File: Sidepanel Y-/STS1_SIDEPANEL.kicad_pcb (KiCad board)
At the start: 2 copper layers, 82.8 x 100 mm, 52 parts, among them IC1 TMP112AQDRLRQ1, J1 Conn_01x08, U1 GUVA-C32SM

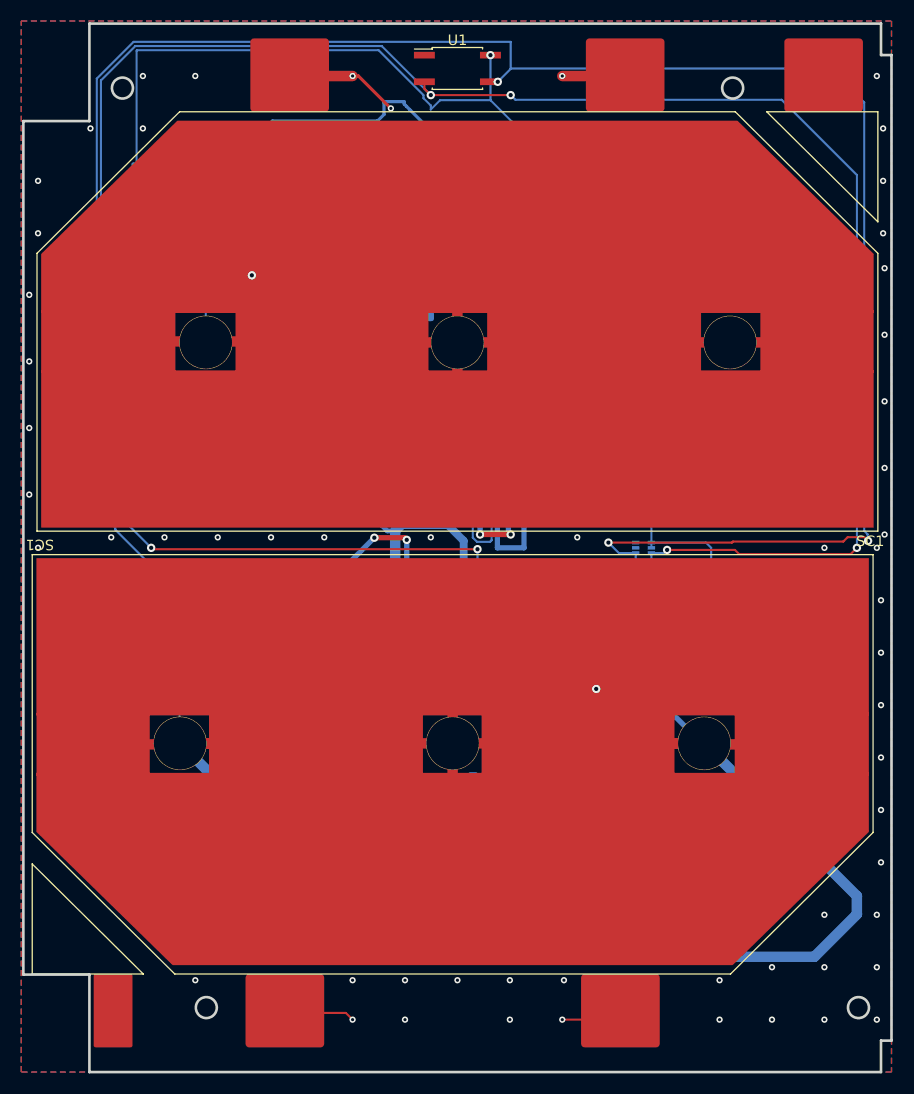
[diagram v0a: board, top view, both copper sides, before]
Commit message: changes to the solar cell footprint + added alternative current sensing solution
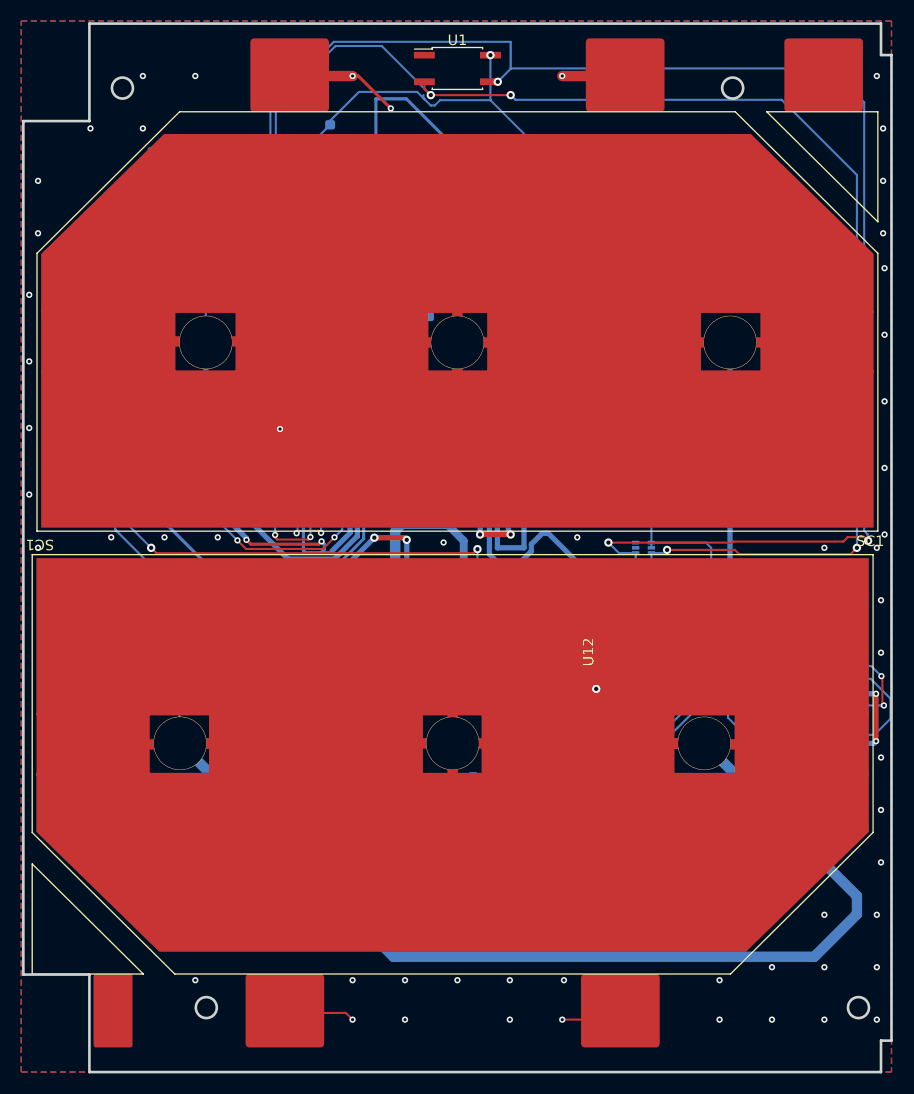
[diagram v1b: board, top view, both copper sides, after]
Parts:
- added R41: 0, Resistor_SMD:R_0603_1608Metric, B.Cu at (108.0, 75.6)
- added R42: 0, Resistor_SMD:R_0603_1608Metric, B.Cu at (141.9, 106.5)
- added R51: 10m, Resistor_SMD:R_0603_1608Metric, B.Cu at (105.2, 75.1)
- added R52: 10m, Resistor_SMD:R_0603_1608Metric, B.Cu at (143.3, 109.2)
- added U11: INA180A4, Package_TO_SOT_SMD:SOT-23-5, B.Cu at (113.1, 79.4)
- added U12: INA180A4, Package_TO_SOT_SMD:SOT-23-5, B.Cu at (134.9, 99.6)
- R21, R22: value tbd -> 330k
- moved C1 18.9 mm to (112.9, 49.9)
- moved UV1 18.0 mm to (107.4, 54.1)
- moved TH1 3.46 mm to (97.1, 52.0)
- moved J1 2.20 mm to (97.4, 58.9)
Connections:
- C_IN1 pad 1: /SolarMPPT/CUR1_OUT -> /SolarMPPT/CUR1_OUT(1)
- C_IN2 pad 1: /SolarMPPT/CUR2_OUT -> /SolarMPPT/CUR2_OUT(1)
- L_IN1 pad 1: /SolarMPPT/CUR1_OUT -> /SolarMPPT/CUR1_OUT(1)
- L_IN2 pad 1: /SolarMPPT/CUR2_OUT -> /SolarMPPT/CUR2_OUT(1)
- R31 pad 2: /SolarMPPT/CUR1_OUT -> /SolarMPPT/CUR1_OUT(1)
- R32 pad 2: /SolarMPPT/CUR2_OUT -> /SolarMPPT/CUR2_OUT(1)
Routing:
- net /SC1_V+: track 130.9 -> 243.2 mm, vias 1 -> 3
- net /SolarMPPT/CUR2_OUT: track 0.00 -> 65.1 mm, vias 0 -> 2
- net /SolarMPPT/CUR2_OUT(1): track 0.00 -> 63.9 mm
- net /SC2_V+: track 291.0 -> 329.0 mm, vias 1 -> 3
- net /SolarMPPT/CUR1_OUT(1): track 0.00 -> 36.1 mm, vias 0 -> 2
- net /SolarMPPT/CUR1_OUT: track 0.00 -> 32.4 mm, vias 0 -> 2
- net /+3V3: track 126.4 -> 96.2 mm
- net /SDA: track 155.0 -> 131.5 mm
- net /SCL: track 174.5 -> 150.9 mm
- net /SC1_I+: track 83.5 -> 61.8 mm, vias 0 -> 2
- net /MPPT1: track 118.1 -> 131.0 mm
- net /SolarMPPT/MPPT1_OUT: track 83.0 -> 95.9 mm
- net /MPPT2: track 129.7 -> 142.5 mm
- net /SC2_I+: track 86.6 -> 89.1 mm
- net /TEMP+: track 4.90 -> 5.44 mm
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- added copper zone on B.Cu, net /SolarMPPT/CUR1_OUT(1)
- added copper zone on B.Cu, net /SolarMPPT/CUR2_OUT(1)
- removed copper zone on B.Cu, net /SolarMPPT/CUR1_OUT
- removed copper zone on B.Cu, net /SolarMPPT/CUR2_OUT

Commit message: added the libraries for the specific components
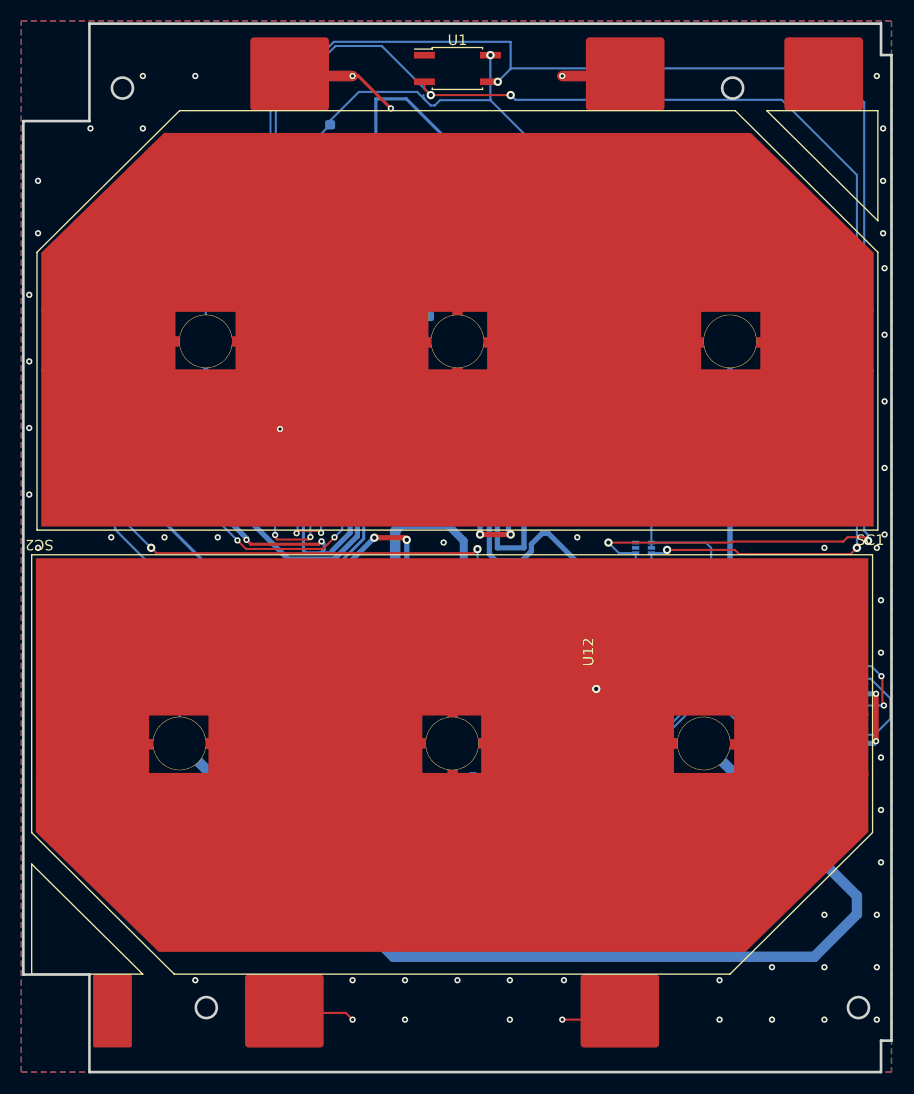
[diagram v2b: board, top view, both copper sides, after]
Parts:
- removed the SC1 at (124.5, 110.1)
- removed the SC1 at (125.0, 67.9)
- added SC1: Solar_Cell, STS_solder:3G30A_40x80_Y_SC1, F.Cu at (125.0, 67.8)
- added SC2: Solar_Cell, STS_solder:3G30A_40x80_Y_SC2, F.Cu at (124.5, 110.2)
- J1: footprint STS_connector:SAMTEC_ZF5S-08-01-T-WT -> STS_Connector:SAMTEC_ZF5S-08-01-T-WT
- UV1: footprint STS_connector:5014610491 -> STS_Connector:5014610491
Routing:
- net /SolarMPPT/CUR2_OUT(1): track 63.9 -> 64.5 mm
